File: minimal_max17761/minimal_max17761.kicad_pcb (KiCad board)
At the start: 4 copper layers, 20.3 x 14 mm, 20 parts, among them U1 MAX17761ATC+

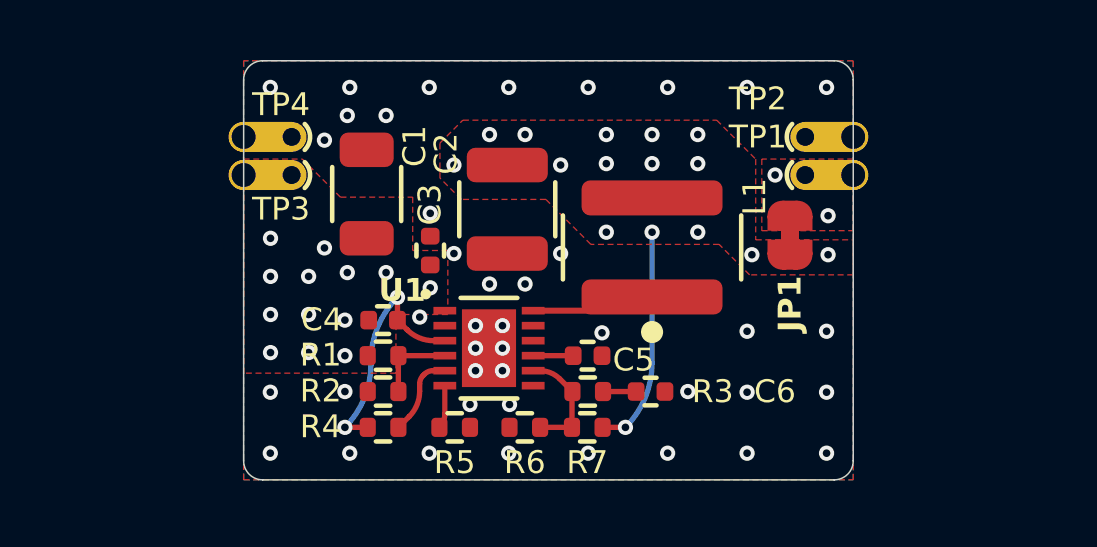
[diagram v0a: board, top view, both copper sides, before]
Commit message: Update minimal_max17761.pdf with formatting adjustments and additional details
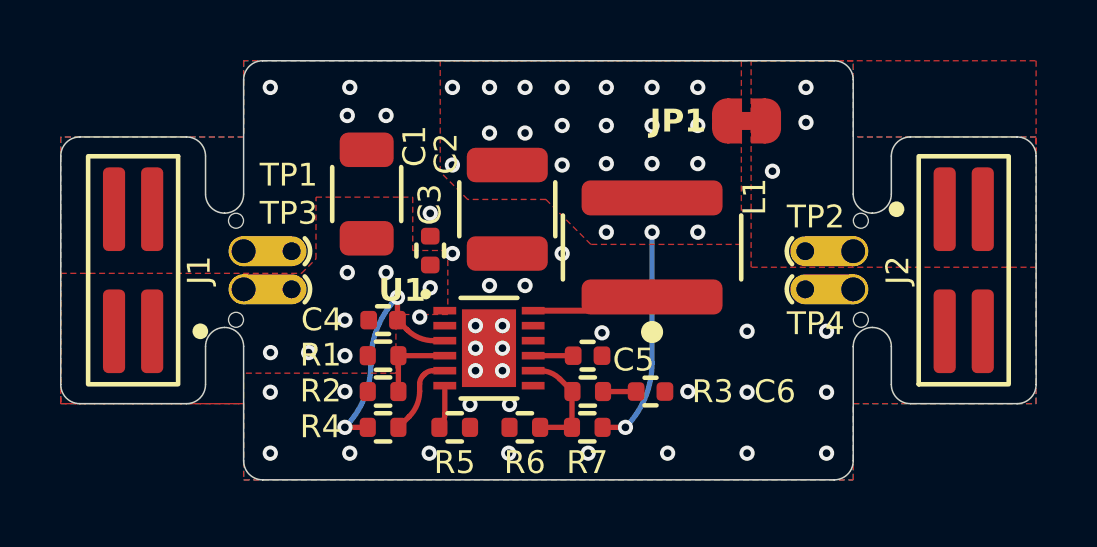
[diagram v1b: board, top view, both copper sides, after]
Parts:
- added J1: FW-02-03-G-D-085-155, connector_footprints:FW-02-03-G-D-085-155, F.Cu at (137.7, 99.9)
- added J2: FW-02-03-G-D-085-155, connector_footprints:FW-02-03-G-D-085-155, F.Cu at (165.4, 99.9)
- added MB1: mouse-bite-midle-50mil-200mil, mouse_bite_footprints:mouse-bite-midle-50mil-200mil, F.Cu at (140.8, 99.9)
- added MB2: mouse-bite-midle-50mil-200mil, mouse_bite_footprints:mouse-bite-midle-50mil-200mil, F.Cu at (162.4, 99.9)
- moved TP4 5.08 mm to (161.7, 100.5)
- moved JP1 4.07 mm to (158.2, 94.9), turned to 0 degrees
- moved TP1 3.81 mm to (141.4, 99.3)
- moved TP3 3.81 mm to (141.4, 100.5)
- moved TP2 2.54 mm to (161.7, 99.3)
- renumbered TP4 to TP1, TP1 to TP2, TP2 to TP4
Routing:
- net GND: vias 42 -> 35
- net /VIN: vias 12 -> 6
- net /3V3_MAX17761: vias 16 -> 22
- net /3V3: vias 2 -> 3
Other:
- board size 20.3 x 14 mm -> 32.5 x 14 mm

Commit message: Add minimal_max17761.glb file for project assets
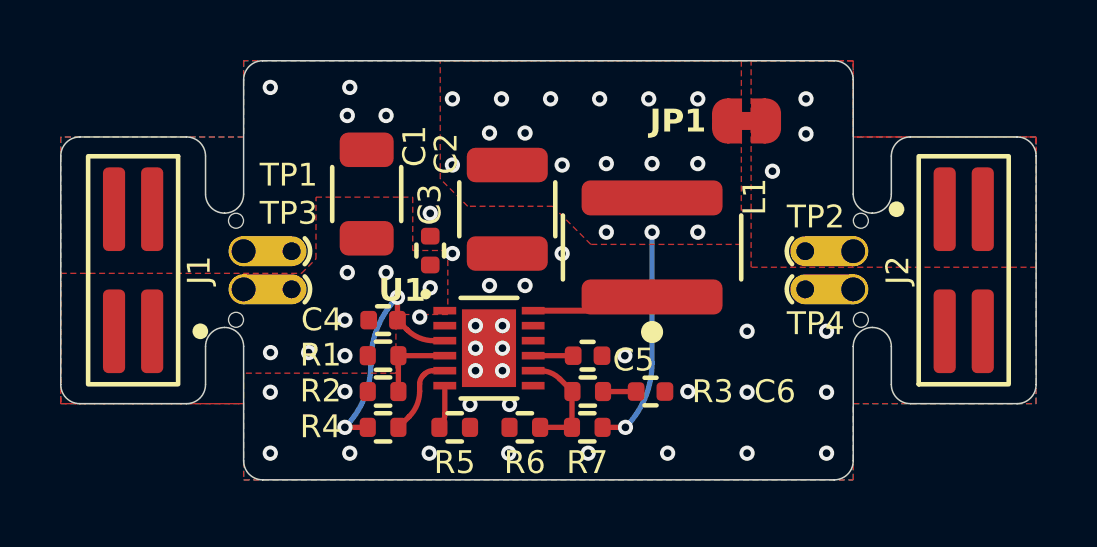
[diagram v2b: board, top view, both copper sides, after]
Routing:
- net /3V3_MAX17761: vias 22 -> 17

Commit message: Update footprint library URIs to use KiCAD_Symbols_Generator
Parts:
- C3, C5: value 0.1uF -> 100 nF
- R4: value 10k -> 10 kΩ

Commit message: Switch to KiCad 9
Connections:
- net Net-(U1-EN/UVLO) renamed /EN/UVLO
- net Net-(U1-RT/SYNC) renamed /RT/SYNC
- net Net-(U1-SS) renamed /SS
- net Net-(U1-VCC) renamed /VCC
- net Net-(U1-~{RESET}) renamed /~{RESET}

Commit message: Backup
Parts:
- moved JP1 2.36 mm to (159.2, 97.1), turned to -90 degrees
- moved J2 1.27 mm to (164.2, 99.9)
- moved MB2 1.27 mm to (161.1, 99.9)
- moved TP2 1.27 mm to (160.5, 99.3)
- moved TP4 1.27 mm to (160.5, 100.5)
- moved R4 1.01 mm to (146.8, 104.4), turned to -90 degrees
- moved R1 0.96 mm to (145.1, 102.7)
- moved R2 0.96 mm to (145.1, 103.9)
- moved C1 0.13 mm to (145.4, 97.4)
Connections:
- net Net-(U1-LX) renamed /LX
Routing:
- net /~{RESET}: track 2.76 -> 1.57 mm
- net /EN/UVLO: track 2.59 -> 3.54 mm
- net GND: vias 35 -> 30
- net /VIN: vias 6 -> 5
- net /3V3_MAX17761: vias 17 -> 11
- net /3V3: vias 3 -> 0
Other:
- board size 32.5 x 14 mm -> 31.2 x 12.7 mm
